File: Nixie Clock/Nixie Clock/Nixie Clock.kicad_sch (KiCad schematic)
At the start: 0 parts

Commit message: More Nixie Stuff
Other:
- removed sheet Rectifier 
- added sheet Microcontroller (Microcontroller.kicad_sch)
- added sheet Tubes (Tubes.kicad_sch)
- sheet Shift Registers ports: added Data Input, Data Latch, Shift Clock, Tube_1_Digit_0, Tube_1_Digit_1, Tube_1_Digit_2, Tube_1_Digit_3, Tube_1_Digit_4, Tube_1_Digit_5, Tube_1_Digit_6, Tube_1_Digit_7, Tube_1_Digit_8, Tube_1_Digit_9, Tube_2_Digit_0, Tube_2_Digit_1, Tube_2_Digit_2, Tube_2_Digit_3, Tube_2_Digit_4, Tube_2_Digit_5, Tube_3_Digit_0, Tube_3_Digit_1, Tube_3_Digit_2, Tube_3_Digit_3, Tube_3_Digit_4, Tube_3_Digit_5, Tube_3_Digit_6, Tube_3_Digit_7, Tube_3_Digit_8, Tube_3_Digit_9, Tube_4_Digit_0, Tube_4_Digit_1, Tube_4_Digit_2, Tube_4_Digit_3, Tube_4_Digit_4, Tube_4_Digit_5, Tube_5_Digit_0, Tube_5_Digit_1, Tube_5_Digit_2, Tube_5_Digit_3, Tube_5_Digit_4, Tube_5_Digit_5, Tube_5_Digit_6, Tube_5_Digit_7, Tube_5_Digit_8, Tube_5_Digit_9, Tube_6_Digit_0, Tube_6_Digit_1, Tube_6_Digit_2; removed none

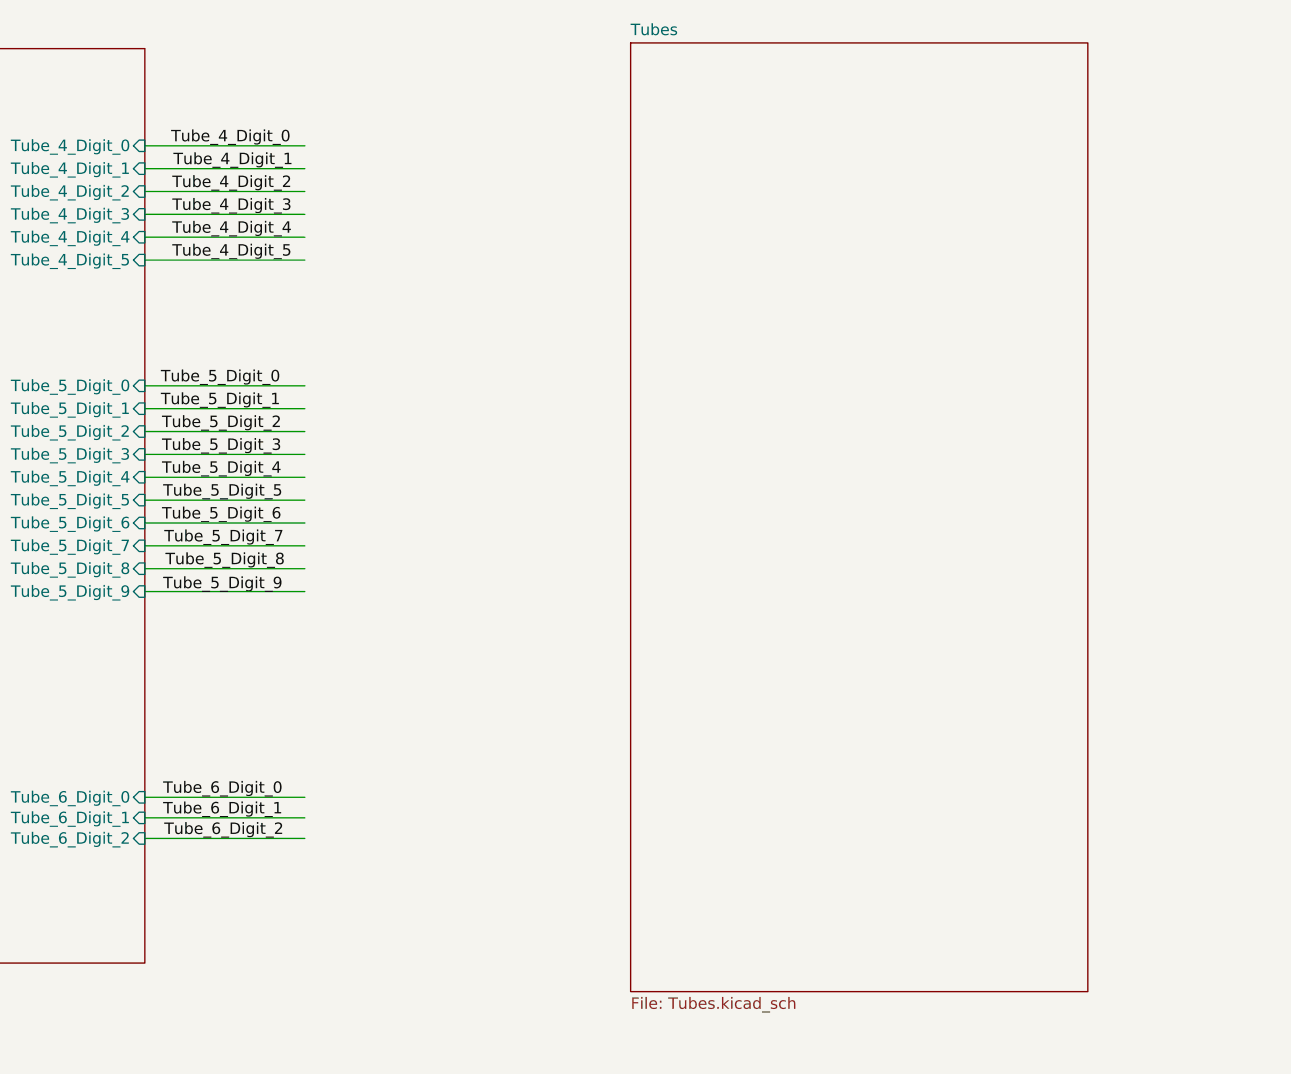
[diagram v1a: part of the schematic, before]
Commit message: Need to add footprints for passives
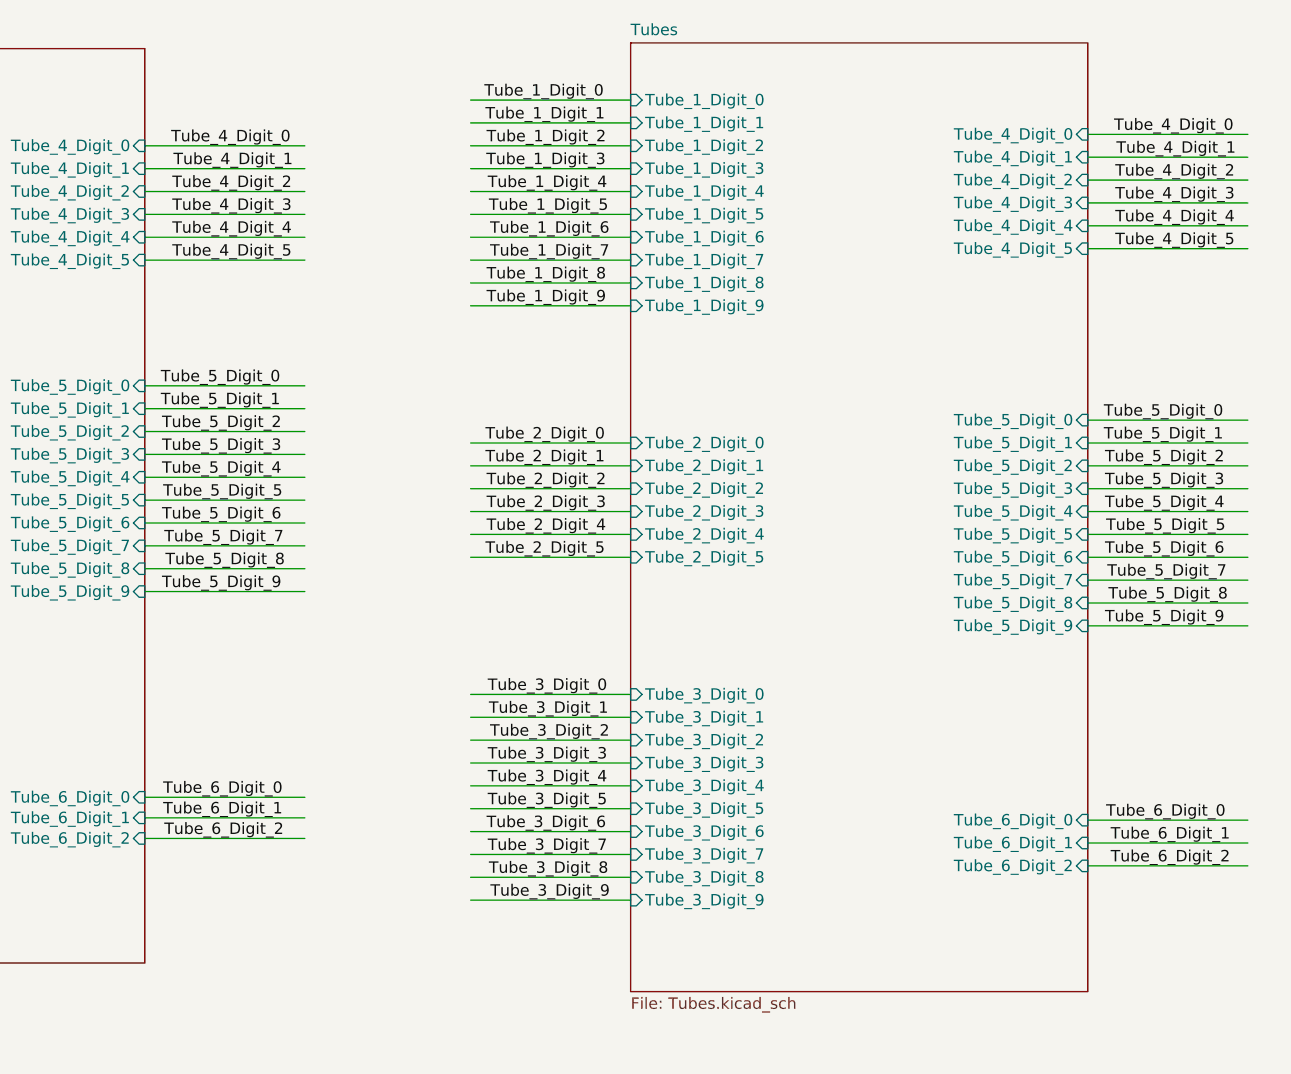
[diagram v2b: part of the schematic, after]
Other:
- sheet Tubes ports: added Tube_1_Digit_0, Tube_1_Digit_1, Tube_1_Digit_2, Tube_1_Digit_3, Tube_1_Digit_4, Tube_1_Digit_5, Tube_1_Digit_6, Tube_1_Digit_7, Tube_1_Digit_8, Tube_1_Digit_9, Tube_2_Digit_0, Tube_2_Digit_1, Tube_2_Digit_2, Tube_2_Digit_3, Tube_2_Digit_4, Tube_2_Digit_5, Tube_3_Digit_0, Tube_3_Digit_1, Tube_3_Digit_2, Tube_3_Digit_3, Tube_3_Digit_4, Tube_3_Digit_5, Tube_3_Digit_6, Tube_3_Digit_7, Tube_3_Digit_8, Tube_3_Digit_9, Tube_4_Digit_0, Tube_4_Digit_1, Tube_4_Digit_2, Tube_4_Digit_3, Tube_4_Digit_4, Tube_4_Digit_5, Tube_5_Digit_0, Tube_5_Digit_1, Tube_5_Digit_2, Tube_5_Digit_3, Tube_5_Digit_4, Tube_5_Digit_5, Tube_5_Digit_6, Tube_5_Digit_7, Tube_5_Digit_8, Tube_5_Digit_9, Tube_6_Digit_0, Tube_6_Digit_1, Tube_6_Digit_2; removed none

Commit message: Added additional parts
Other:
- added sheet LEDS (LEDS.kicad_sch)
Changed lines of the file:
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@@
+    )
+  )
+  (sheet (at 24.13 70.485) (size 34.925 19.685) (fields_autoplaced)
+    (stroke (width 0.1524) (type solid) (color 0 0 0 0))
+    (fill (color 0 0 0 0.0000))
+    (property "Sheet name" "LEDS" (id 0) (at 24.13 69.7734 0)
+      (effects (font (size 1.27 1.27)) (justify left bottom))
+    )
+    (property "Sheet file" "LEDS.kicad_sch" (id 1) (at 24.13 90.7546 0)
+      (effects (font (size 1.27 1.27)) (justify left top))
     )
   )
@@
     (path "/5cd16da4-e618-43c4-b383-b5cc3d0967ec" (page "5"))
     (path "/2d6ba7e3-0697-4cb0-9be8-f585776c6780" (page "5"))
+    (path "/7c18b937-ca7b-4a8e-814f-b4e20058c69b" (page "6"))
   )
   (symbol_instances
@@
       (reference "#PWR074") (unit 1) (value "VDC") (footprint "")
     )
+    (path "/7c18b937-ca7b-4a8e-814f-b4e20058c69b/d56efe5f-34c3-4321-a406-c700d177cf6e"
+      (reference "#PWR075") (unit 1) (value "GND") (footprint "")
+    )
+    (path "/7c18b937-ca7b-4a8e-814f-b4e20058c69b/2749e17a-f156-44ff-8d7f-2806762d6379"
+      (reference "#PWR076") (unit 1) (value "+12V") (footprint "")
+    )
+    (path "/7c18b937-ca7b-4a8e-814f-b4e20058c69b/de9bc619-c4df-411e-932d-bcd4e88ff07f"
+      (reference "#PWR077") (unit 1) (value "GND") (footprint "")
+    )
+    (path "/7c18b937-ca7b-4a8e-814f-b4e20058c69b/a974e56b-6bdf-4012-94ec-89ee905530b7"
+      (reference "#PWR078") (unit 1) (value "+12V") (footprint "")
+    )
+    (path "/7c18b937-ca7b-4a8e-814f-b4e20058c69b/18314eb2-fd29-4b16-9178-dce60e70d0c3"
+      (reference "#PWR079") (unit 1) (value "GND") (footprint "")
+    )
+    (path "/7c18b937-ca7b-4a8e-814f-b4e20058c69b/1bd63f2f-ea58-49a5-bdb9-19e3a342ddfa"
+      (reference "#PWR080") (unit 1) (value "+12V") (footprint "")
+    )
+    (path "/7c18b937-ca7b-4a8e-814f-b4e20058c69b/0e0602f4-ac67-486b-8080-6f6a71bcaa27"
+      (reference "#PWR081") (unit 1) (value "GND") (footprint "")
+    )
+    (path "/7c18b937-ca7b-4a8e-814f-b4e20058c69b/24e2c8dc-d1ec-4b3c-8f5d-17d6f9178996"
+      (reference "#PWR082") (unit 1) (value "GND") (footprint "")
+    )
+    (path "/7c18b937-ca7b-4a8e-814f-b4e20058c69b/b4ecea00-1db5-44fe-9fe0-3b6f531d359b"
+      (reference "#PWR083") (unit 1) (value "GND") (footprint "")
+    )
+    (path "/7c18b937-ca7b-4a8e-814f-b4e20058c69b/67a742f7-2770-4469-98d0-1f2d515cec07"
+      (reference "#PWR084") (unit 1) (value "GND") (footprint "")
+    )
+    (path "/7c18b937-ca7b-4a8e-814f-b4e20058c69b/b3958deb-4115-4237-9e2e-c6cf500ce3a4"
+      (reference "#PWR085") (unit 1) (value "GND") (footprint "")
+    )
+    (path "/7c18b937-ca7b-4a8e-814f-b4e20058c69b/50fffb15-925c-472d-9964-315330e5bc38"
+      (reference "#PWR086") (unit 1) (value "GND") (footprint "")
+    )
     (path "/4c0a6173-3bb5-488a-ae98-333b4befcac8/501e031b-1e2a-414e-991e-bb05f5921dbc"
       (reference "C1") (unit 1) (value "10uF") (footprint "Capacitor_THT:CP_Radial_D6.3mm_P2.50mm")
@@
       (reference "D2") (unit 1) (value "BAV21") (footprint "Diode_THT:D_DO-35_SOD27_P7.62mm_Horizontal")
     )
+    (path "/7c18b937-ca7b-4a8e-814f-b4e20058c69b/741d7623-cf63-4dae-a654-2b503453e65e"
+      (reference "D3") (unit 1) (value "LED_RGB") (footprint "CLY6D-FKC-CK1N1D1BB7D3D3:CLY6D-FKC-CK1N1D1BB7D3D3")
+    )
+    (path "/7c18b937-ca7b-4a8e-814f-b4e20058c69b/660ae773-4812-4bf2-b735-1635c5e0c0b3"
+      (reference "D4") (unit 1) (value "LED_RGB") (footprint "CLY6D-FKC-CK1N1D1BB7D3D3:CLY6D-FKC-CK1N1D1BB7D3D3")
+    )
+    (path "/7c18b937-ca7b-4a8e-814f-b4e20058c69b/165a8d59-db7c-455b-a822-c194b8892552"
+      (reference "D5") (unit 1) (value "LED_RGB") (footprint "CLY6D-FKC-CK1N1D1BB7D3D3:CLY6D-FKC-CK1N1D1BB7D3D3")
+    )
+    (path "/7c18b937-ca7b-4a8e-814f-b4e20058c69b/79733a0f-949f-4b59-bad7-0eccf626ec52"
+      (reference "D6") (unit 1) (value "LED_RGB") (footprint "CLY6D-FKC-CK1N1D1BB7D3D3:CLY6D-FKC-CK1N1D1BB7D3D3")
+    )
+    (path "/7c18b937-ca7b-4a8e-814f-b4e20058c69b/2bc028ef-6bd8-432b-87de-1ae01e491006"
+      (reference "D7") (unit 1) (value "LED_RGB") (footprint "CLY6D-FKC-CK1N1D1BB7D3D3:CLY6D-FKC-CK1N1D1BB7D3D3")
+    )
+    (path "/7c18b937-ca7b-4a8e-814f-b4e20058c69b/f2e6fa7e-5232-430f-b3a6-3aee2dd7138b"
+      (reference "D8") (unit 1) (value "LED_RGB") (footprint "CLY6D-FKC-CK1N1D1BB7D3D3:CLY6D-FKC-CK1N1D1BB7D3D3")
+    )
+    (path "/7c18b937-ca7b-4a8e-814f-b4e20058c69b/6b4fb8df-f2b2-4c33-863e-aa7d186bda22"
+      (reference "H1") (unit 1) (value "MountingHole") (footprint "MountingHole:MountingHole_4.3mm_M4")
+    )
+    (path "/7c18b937-ca7b-4a8e-814f-b4e20058c69b/f94802d7-b31d-4d1a-be98-fc6a42c4b2a4"
+      (reference "H2") (unit 1) (value "MountingHole") (footprint "MountingHole:MountingHole_4.3mm_M4")
+    )
+    (path "/7c18b937-ca7b-4a8e-814f-b4e20058c69b/25a83e32-6d89-49ed-96ee-3270767769d9"
+      (reference "H3") (unit 1) (value "MountingHole") (footprint "MountingHole:MountingHole_4.3mm_M4")
+    )
+    (path "/7c18b937-ca7b-4a8e-814f-b4e20058c69b/2f1440fe-b315-45a3-8005-f3762d97f9b3"
+      (reference "H4") (unit 1) (value "MountingHole") (footprint "MountingHole:MountingHole_4.3mm_M4")
+    )
     (path "/4c0a6173-3bb5-488a-ae98-333b4befcac8/b75e6d15-4d7a-4aec-ab57-dc77af04a9b9"
       (reference "J1") (unit 1) (value "PJ-202A") (footprint "digikey-footprints:Barrel_Jack_5.5mmODx2.1mmID_PJ-202A")
@@
     )
     (path "/4c0a6173-3bb5-488a-ae98-333b4befcac8/c9f3ebbe-eccc-4121-ad6d-5923dc41f2d2"
-      (reference "Q1") (unit 1) (value "MPSA55") (footprint "MPSA55:TO92127P520H787-3")
+      (reference "Q1") (unit 1) (value "MPSA55") (footprint "Package_TO_SOT_THT:TO-92_Inline")
     )
     (path "/4c0a6173-3bb5-488a-ae98-333b4befcac8/46107e03-7b11-452f-8c51-f0b79c86cd35"
@@
       (reference "R21") (unit 1) (value "14k") (footprint "Resistor_THT:R_Axial_DIN0204_L3.6mm_D1.6mm_P7.62mm_Horizontal")
     )
+    (path "/7c18b937-ca7b-4a8e-814f-b4e20058c69b/2e0e39d4-7584-4cdd-8749-f86fe65ad280"
+      (reference "R22") (unit 1) (value "Resistor_THT:R_Axial_DIN0207_L6.3mm_D2.5mm_P10.16mm_Horizontal") (footprint "Resistor_THT:R_Axial_DIN0207_L6.3mm_D2.5mm_P10.16mm_Horizontal")
+    )
+    (path "/7c18b937-ca7b-4a8e-814f-b4e20058c69b/c0608093-49f2-4e45-88c6-91d1f34036a0"
+      (reference "R23") (unit 1) (value "110") (footprint "Resistor_THT:R_Axial_DIN0411_L9.9mm_D3.6mm_P12.70mm_Horizontal")
+    )
+    (path "/7c18b937-ca7b-4a8e-814f-b4e20058c69b/d450a081-e748-4967-bdd7-7d5dcd4217c6"
+      (reference "R24") (unit 1) (value "Resistor_THT:R_Axial_DIN0207_L6.3mm_D2.5mm_P10.16mm_Horizontal") (footprint "Resistor_THT:R_Axial_DIN0207_L6.3mm_D2.5mm_P10.16mm_Horizontal")
+    )
+    (path "/7c18b937-ca7b-4a8e-814f-b4e20058c69b/59447725-3768-4d52-b642-e426f03b277a"
+      (reference "R25") (unit 1) (value "150") (footprint "Resistor_THT:R_Axial_DIN0414_L11.9mm_D4.5mm_P15.24mm_Horizontal")
+    )
+    (path "/7c18b937-ca7b-4a8e-814f-b4e20058c69b/87150481-8afc-42c1-a281-e8c8f5a861ca"
+      (reference "R26") (unit 1) (value "Resistor_THT:R_Axial_DIN0207_L6.3mm_D2.5mm_P10.16mm_Horizontal") (footprint "Resistor_THT:R_Axial_DIN0207_L6.3mm_D2.5mm_P10.16mm_Horizontal")
+    )
+    (path "/7c18b937-ca7b-4a8e-814f-b4e20058c69b/1b9d866c-7fe6-47ba-9ec0-8145608fccd9"
+      (reference "R27") (unit 1) (value "150") (footprint "Resistor_THT:R_Axial_DIN0414_L11.9mm_D4.5mm_P15.24mm_Horizontal")
+    )
+    (path "/7c18b937-ca7b-4a8e-814f-b4e20058c69b/05919a82-f89e-4ffe-b4f5-999349525613"
+      (reference "RV1") (unit 1) (value "10K") (footprint "WH148:WH148")
+    )
+    (path "/7c18b937-ca7b-4a8e-814f-b4e20058c69b/61b01b10-88cf-427d-abab-2f7cd7870871"
+      (reference "RV2") (unit 1) (value "10K") (footprint "WH148:WH148")
+    )
+    (path "/7c18b937-ca7b-4a8e-814f-b4e20058c69b/0575a02d-3fd9-4fbf-a282-8f7ab8b20a7e"
+      (reference "RV3") (unit 1) (value "10K") (footprint "WH148:WH148")
+    )
     (path "/5cd16da4-e618-43c4-b383-b5cc3d0967ec/4a9e95d3-7761-4e6f-b896-f671783f571b"
